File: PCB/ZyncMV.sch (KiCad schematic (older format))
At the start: 0 parts

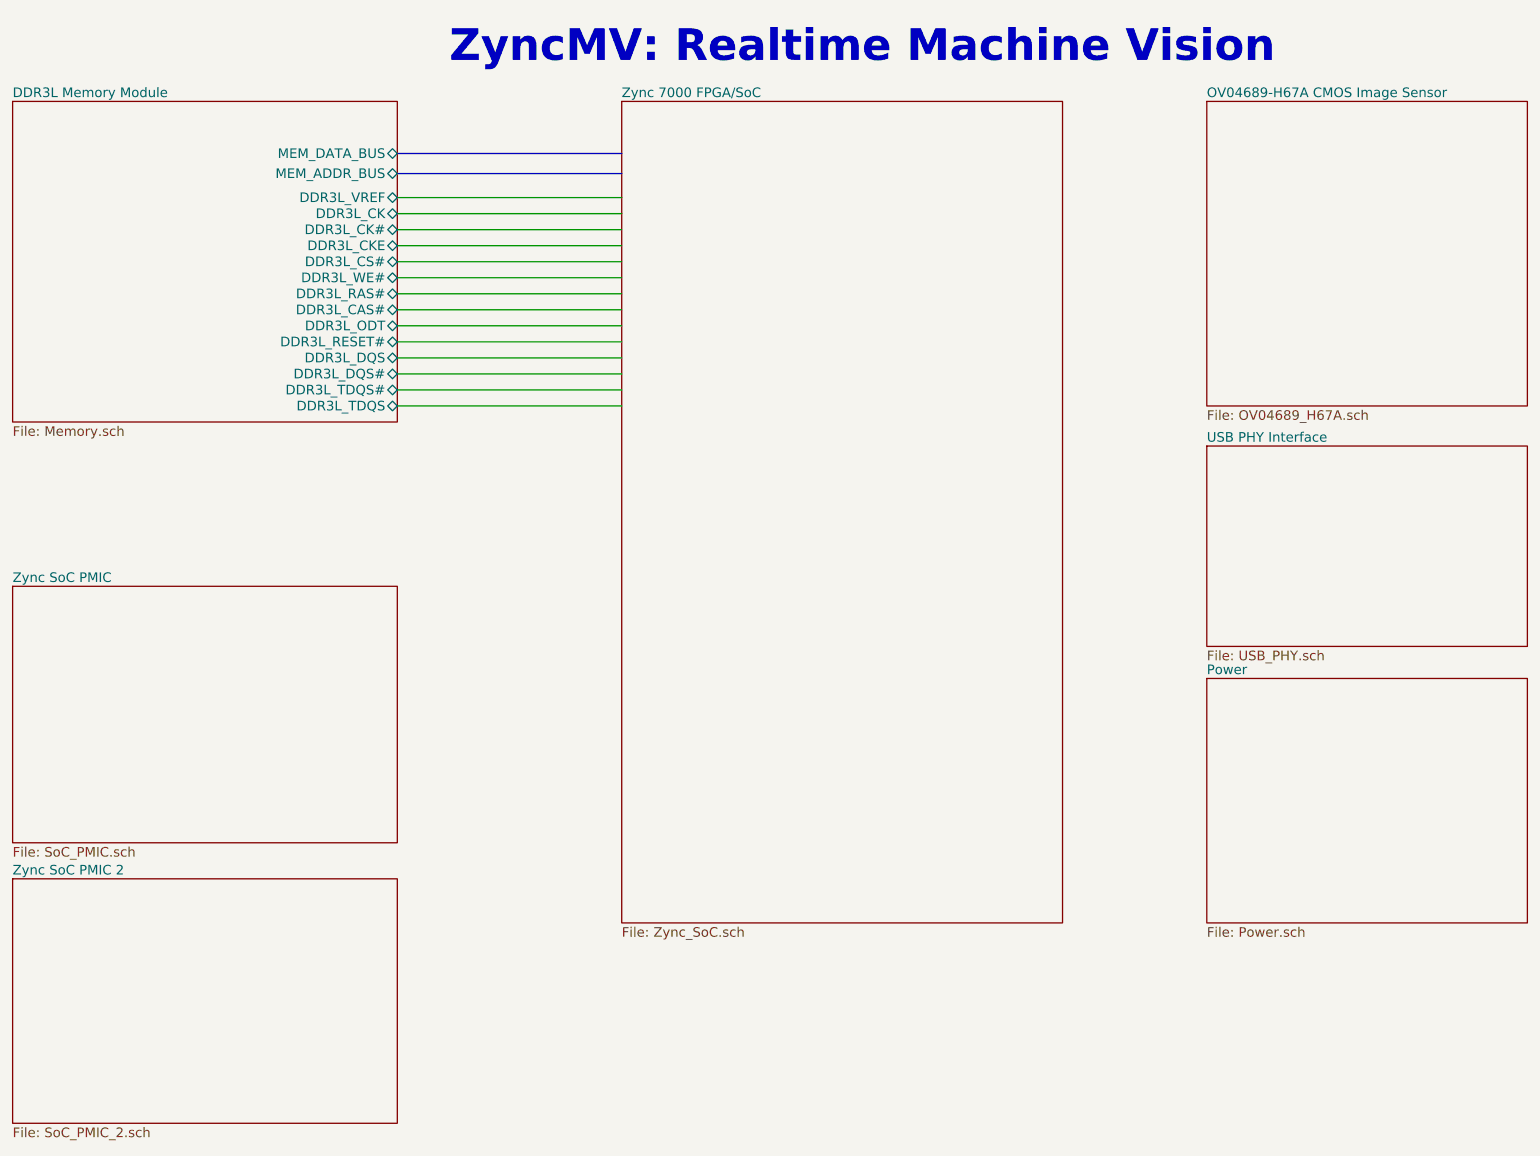
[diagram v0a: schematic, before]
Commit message: USB
This commit contains mostly work done to the USB sections. Theres a FTDI
chip for USB coms and programmign and an USB transceiver/PHY for usb
perfipherals or daisychaining devices.  Also the termiantion resistors
have been removed from the memory since termination can be set on DDR
pins of the FPGA with verilog.
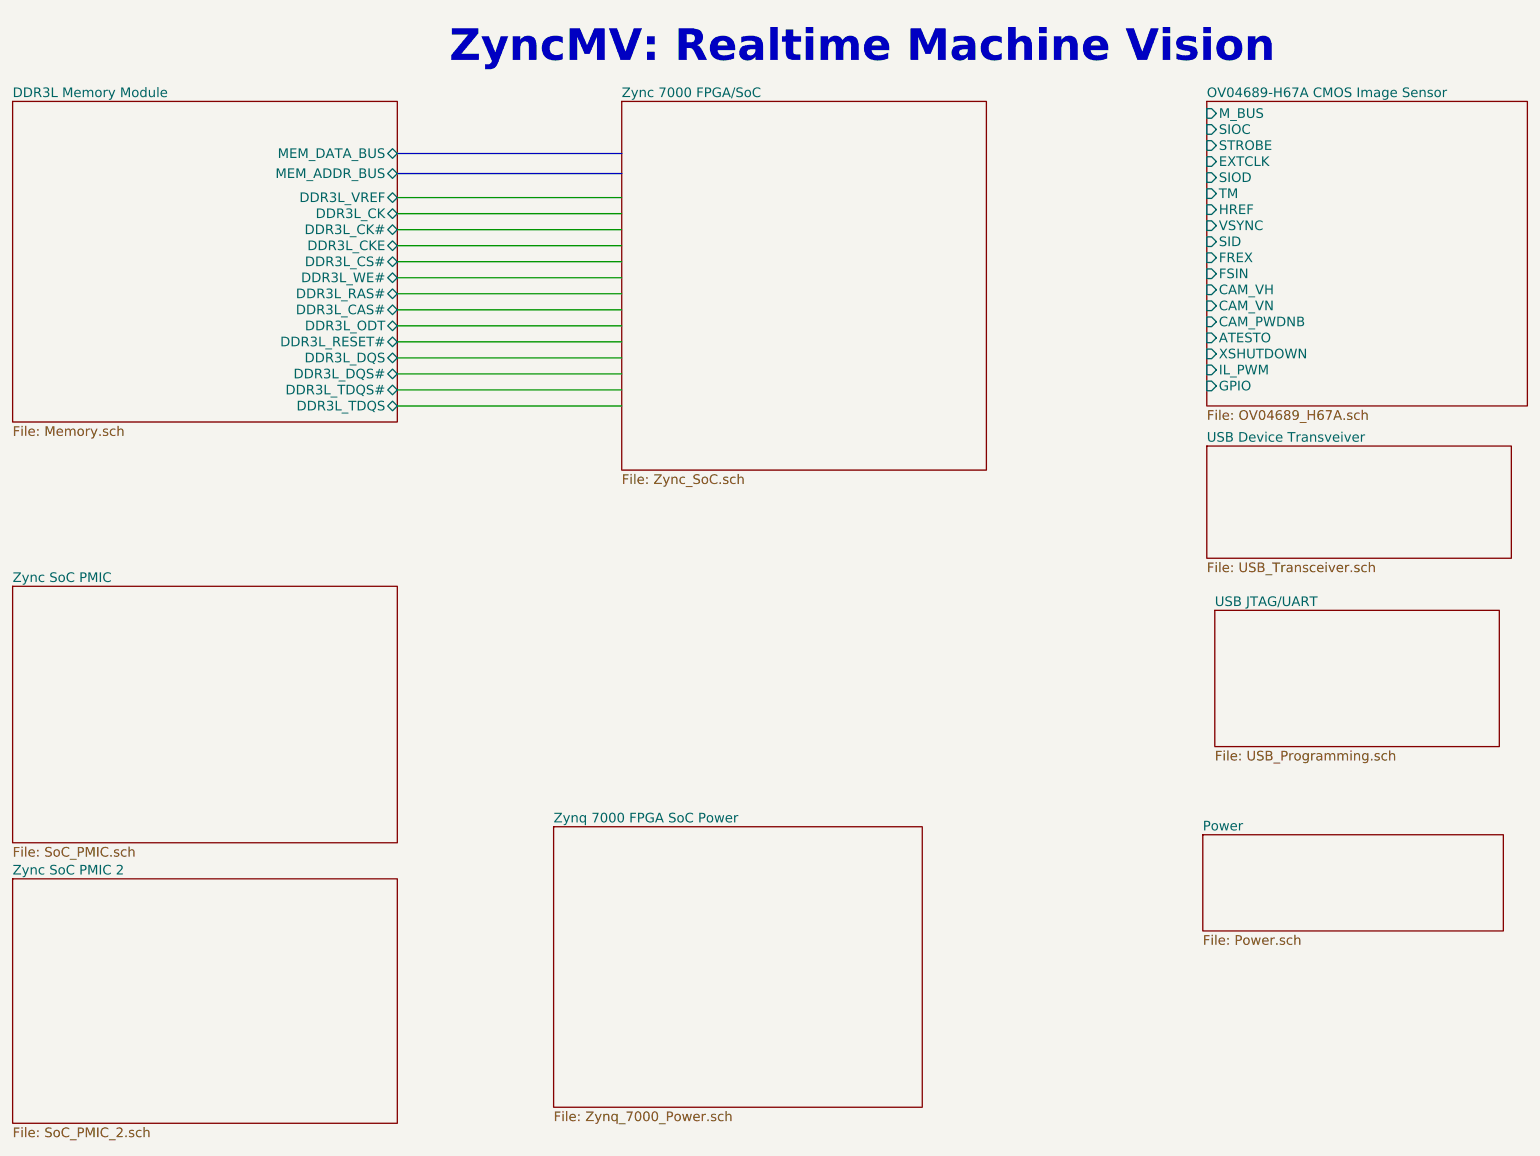
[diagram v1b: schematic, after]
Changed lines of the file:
@@
 $Descr A4 11693 8268
 encoding utf-8
-Sheet 1 8
+Sheet 1 10
 Title ""
 Date "2016-12-23"
@@
 $EndDescr
 $Sheet
-S 4700 1275 2750 5125
+S 4700 1275 2275 2300
 U 585AE0B8
 F0 "Zync 7000 FPGA/SoC" 60
@@
 $EndSheet
 $Sheet
-S 8350 4875 2000 1525
+S 8325 5850 1875 600
 U 585AE0DE
 F0 "Power" 60
@@
 F0 "OV04689-H67A CMOS Image Sensor" 60
 F1 "OV04689_H67A.sch" 60
+F2 "M_BUS" I L 8350 1350 60
+F3 "SIOC" I L 8350 1450 60
+F4 "STROBE" I L 8350 1550 60
+F5 "EXTCLK" I L 8350 1650 60
+F6 "SIOD" I L 8350 1750 60
+F7 "TM" I L 8350 1850 60
+F8 "HREF" I L 8350 1950 60
+F9 "VSYNC" I L 8350 2050 60
+F10 "SID" I L 8350 2150 60
+F11 "FREX" I L 8350 2250 60
+F12 "FSIN" I L 8350 2350 60
+F13 "CAM_VH" I L 8350 2450 60
+F14 "CAM_VN" I L 8350 2550 60
+F15 "CAM_PWDNB" I L 8350 2650 60
+F16 "ATESTO" I L 8350 2750 60
+F17 "XSHUTDOWN" I L 8350 2850 60
+F18 "GPIO" I L 8350 3050 60
+F19 "IL_PWM" I L 8350 2950 60
 $EndSheet
 $Sheet
@@
 $EndSheet
 $Sheet
-S 8350 3425 2000 1250
+S 8350 3425 1900 700
 U 585AE27C
-F0 "USB PHY Interface" 60
-F1 "USB_PHY.sch" 60
+F0 "USB Device Transveiver" 60
+F1 "USB_Transceiver.sch" 60
 $EndSheet
 Text Notes 3625 1050 0    197  ~ 39
@@
 Wire Wire Line
 	3300 3175 4700 3175
+$Sheet
+S 4275 5800 2300 1750
+U 5895E8EF
+F0 "Zynq 7000 FPGA SoC Power" 60
+F1 "Zynq_7000_Power.sch" 60
+$EndSheet
+$Sheet
+S 8400 4450 1775 850
+U 5898ADD6
+F0 "USB JTAG/UART" 60
+F1 "USB_Programming.sch" 60
+$EndSheet
 $EndSCHEMATC

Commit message: Power Topology change
Switching to a new PMIC TPS65400RGZR, has a much more compact PCB layout
and will provide all the necessary voltages for the system.
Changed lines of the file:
@@
 EESchema Schematic File Version 2
+LIBS:ZyncMV-rescue
 LIBS:power
 LIBS:device
@@
 $Descr A4 11693 8268
 encoding utf-8
-Sheet 1 10
+Sheet 1 9
 Title ""
 Date "2016-12-23"
@@
 Text Notes 3625 1050 0    197  ~ 39
 ZyncMV: Realtime Machine Vision
-$Sheet
-S 900  4300 2400 1600
-U 5878744A
-F0 "Zync SoC PMIC" 60
-F1 "SoC_PMIC.sch" 60
-$EndSheet
-$Sheet
-S 900  6125 2400 1525
-U 5878DB5C
-F0 "Zync SoC PMIC 2" 60
-F1 "SoC_PMIC_2.sch" 60
-$EndSheet
 Wire Bus Line
 	3300 1600 4700 1600
@@
 F1 "USB_Programming.sch" 60
 $EndSheet
+$Sheet
+S 1125 4500 1975 1825
+U 5897FD81
+F0 "SoC PMIC - TPS65400RGZR" 60
+F1 "PMIC_TPS65400RGZR.sch" 60
+$EndSheet
 $EndSCHEMATC
